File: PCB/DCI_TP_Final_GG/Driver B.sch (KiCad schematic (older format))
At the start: 18 parts, among them J301 DRIVER B OUT, U301 A3967

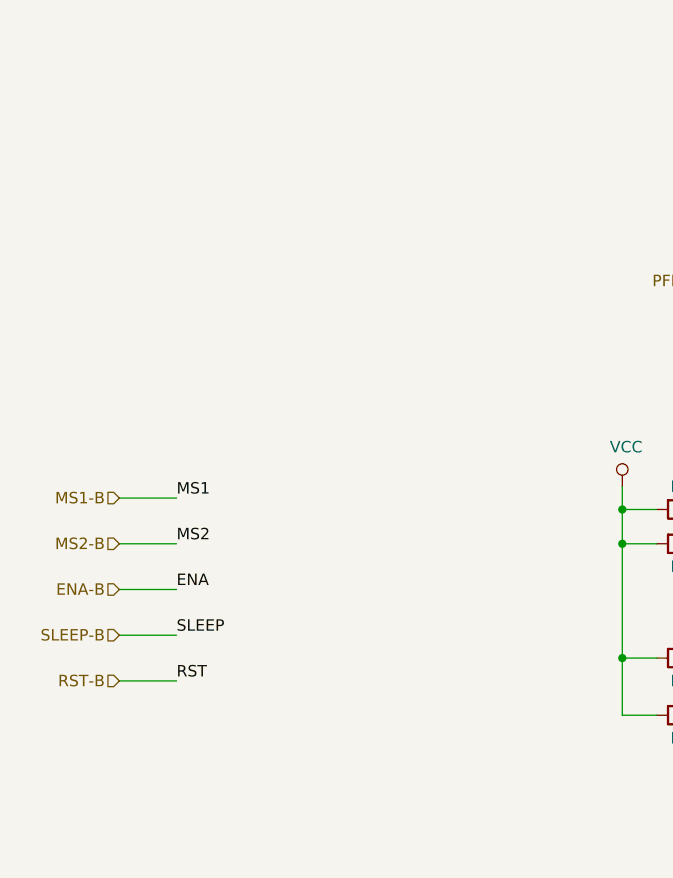
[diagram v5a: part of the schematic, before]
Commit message: Cambio de ubicacion de capacitores de desacople en la jerarquia del esquematico y actualizacion de identificadores en PCB
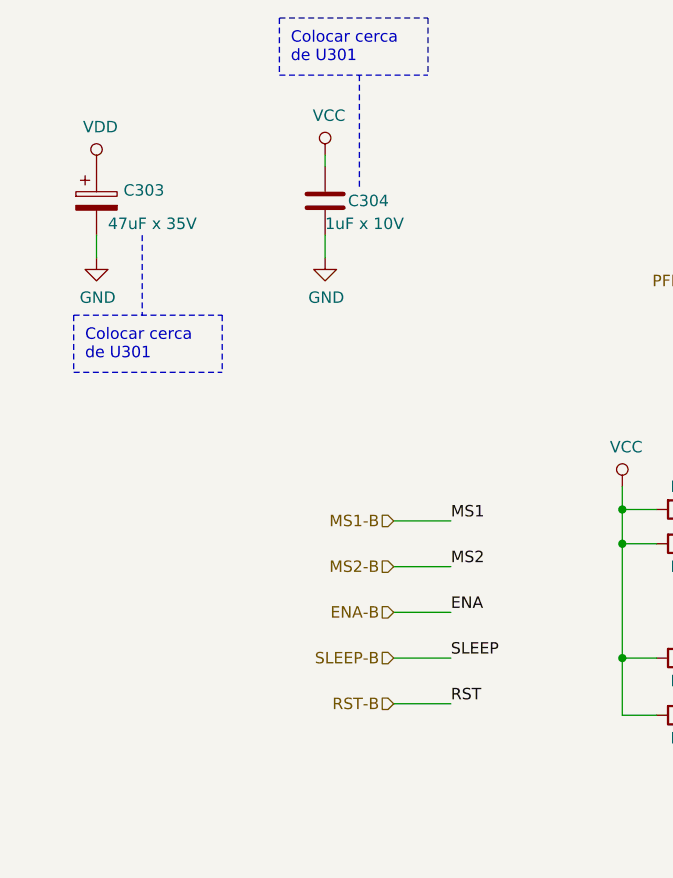
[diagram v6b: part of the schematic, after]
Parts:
- added C303: 47uF x 35V, Capacitor_THT:CP_Radial_D5.0mm_P2.00mm, symbol Device:CP
- added C304: 1uF x 10V, Capacitor_SMD:C_0805_2012Metric, symbol Device:C
- U301: footprint Package_SO:SOIC-24W_7.5x15.4mm_P1.27mm -> DCI_TP_Final_GG:SOIC-24W_7.5x15.4mm_P1.27mm
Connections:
- net GND: now also C303.2, C304.2
- net VCC: now also C304.1
- net VDD: now also C303.1
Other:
- note added: "Colocar cerca\nde U301\n"
